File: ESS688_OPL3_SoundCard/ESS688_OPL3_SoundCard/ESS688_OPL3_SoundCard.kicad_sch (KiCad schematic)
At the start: 1 part, among them J1 Bus_ISA_16bit

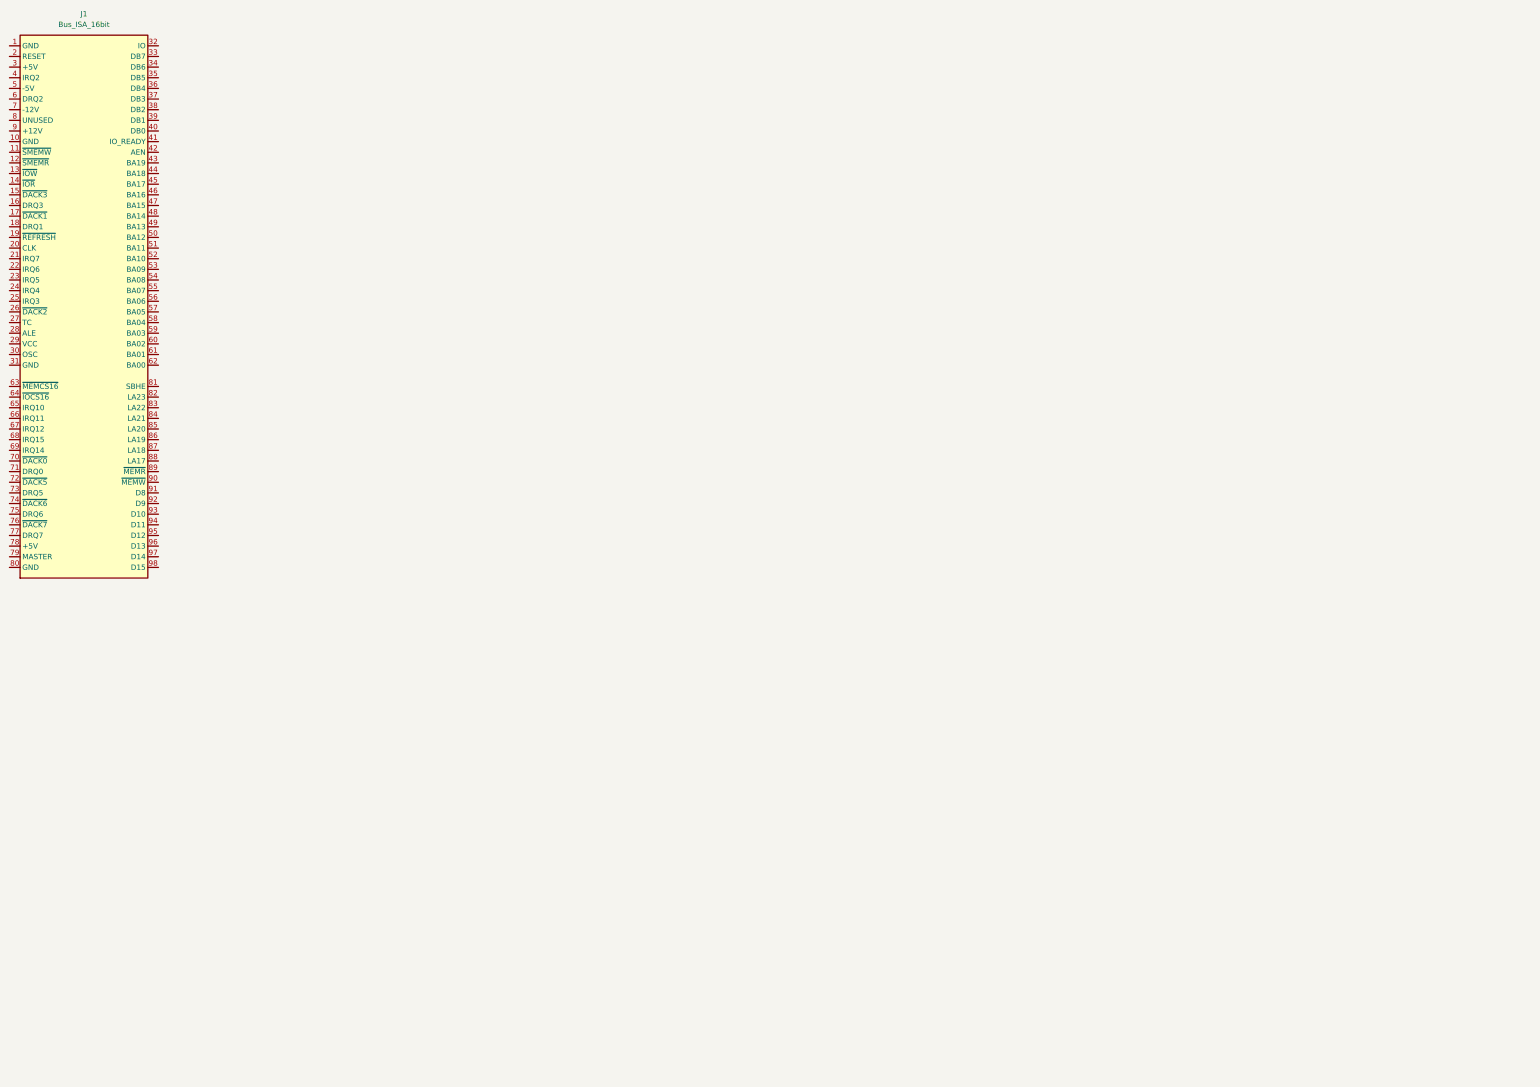
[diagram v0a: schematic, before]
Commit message: ES688 symbol updated, added more symbols to schematic
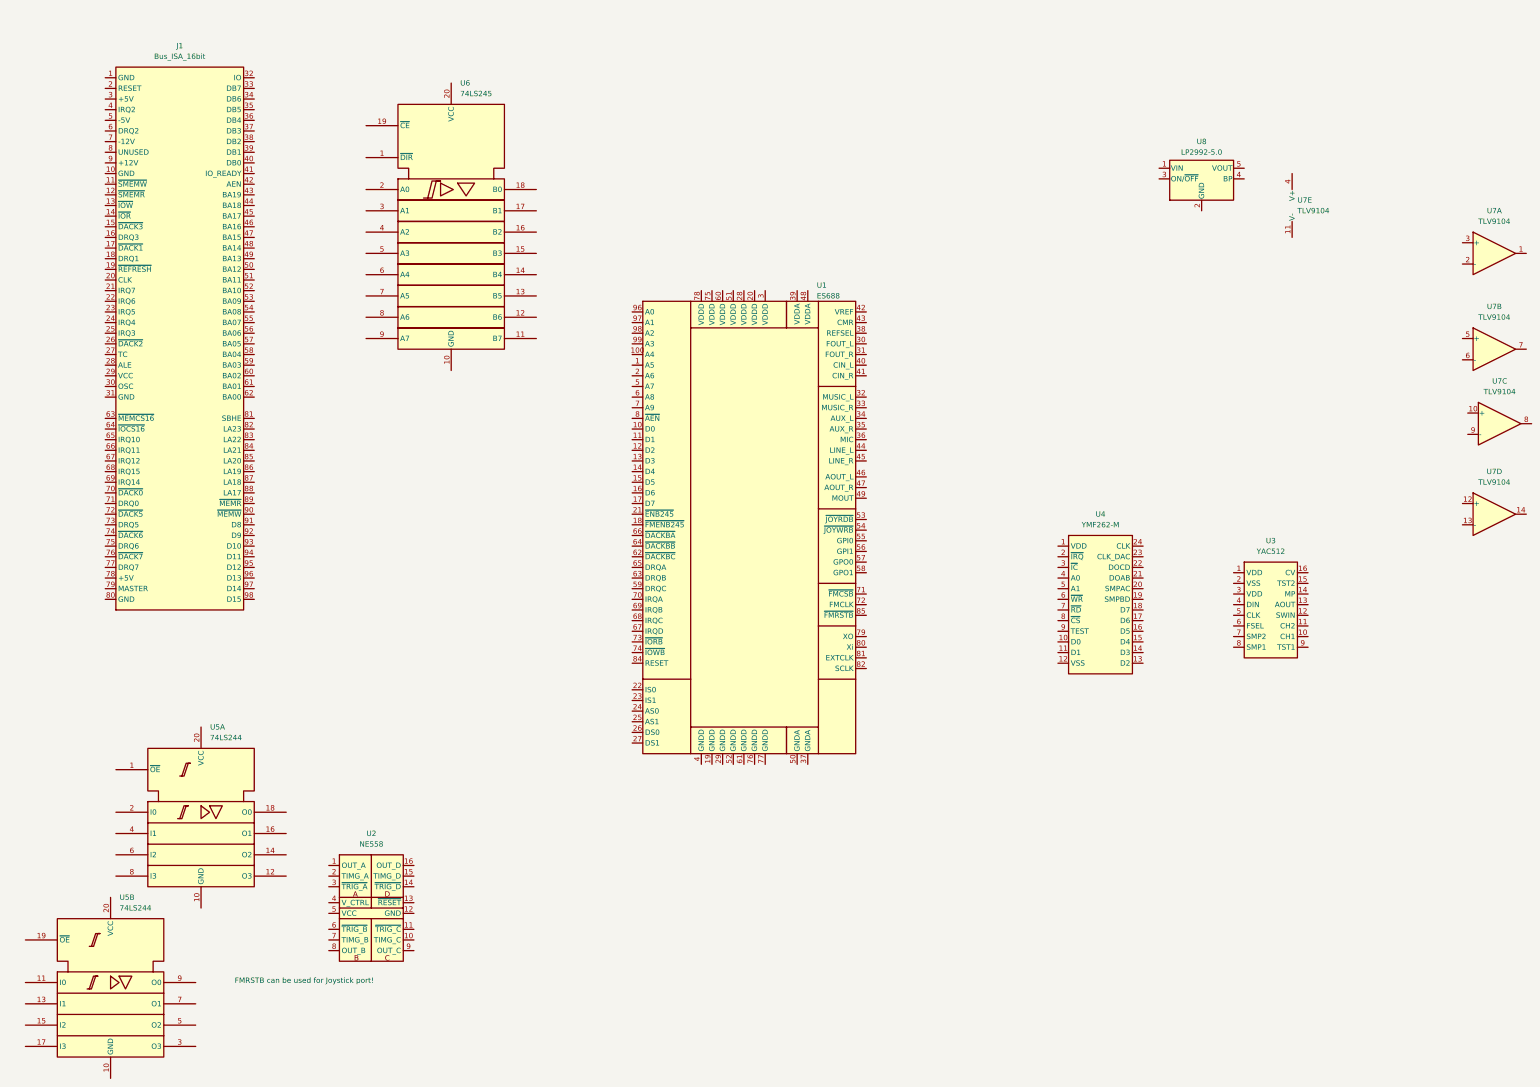
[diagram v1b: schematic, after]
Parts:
- added U1: ES688, Package_QFP:PQFP-100_14x20mm_P0.65mm, symbol ESS688_OPL3_SoundCard:ES688
- added U2: NE558, Package_DIP:DIP-16_W7.62mm, symbol ESS688_OPL3_SoundCard:NE558
- added U3: YAC512, Package_SO:SO-16_5.3x10.2mm_P1.27mm, symbol ESS688_OPL3_SoundCard:YAC512
- added U4: YMF262-M, Package_SO:SOP-24_7.5x15.4mm_P1.27mm, symbol ESS688_OPL3_SoundCard:YMF262-M
- added U5: 74LS244, Package_TO_SOT_SMD:SOT-23-5, symbol 74xx_IEEE:74LS244
- added U6: 74LS245, symbol 74xx_IEEE:74LS245
- added U7: TLV9104, Package_DFN_QFN:Texas_DSQ0010A_WSON-10-1EP_2x2mm_P0.4mm_EP0.9x1.5mm, symbol Amplifier_Operational:TL084
- added U8: LP2992-5.0, Package_TO_SOT_SMD:SOT-23-5, symbol Regulator_Linear:LP2985-5.0
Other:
- note added: "FMRSTB can be used for Joystick port!"
- moved on the sheet: J1

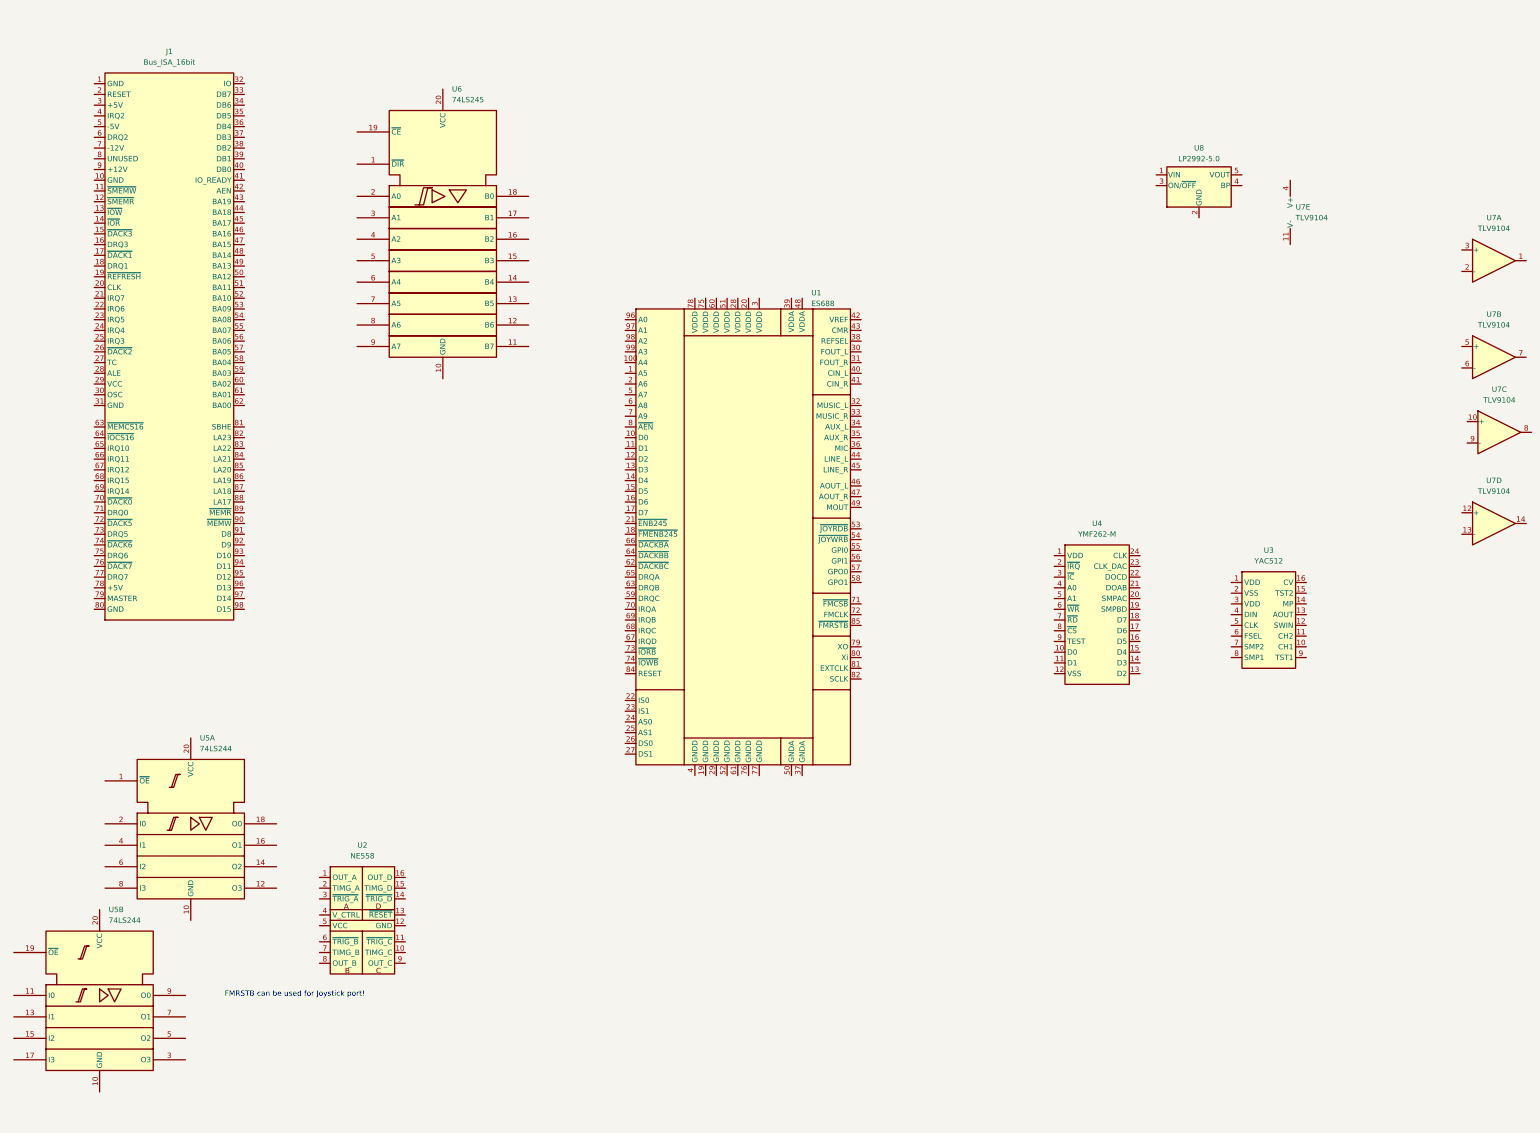
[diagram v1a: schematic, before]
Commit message: busses drawn, digital part 90% finished
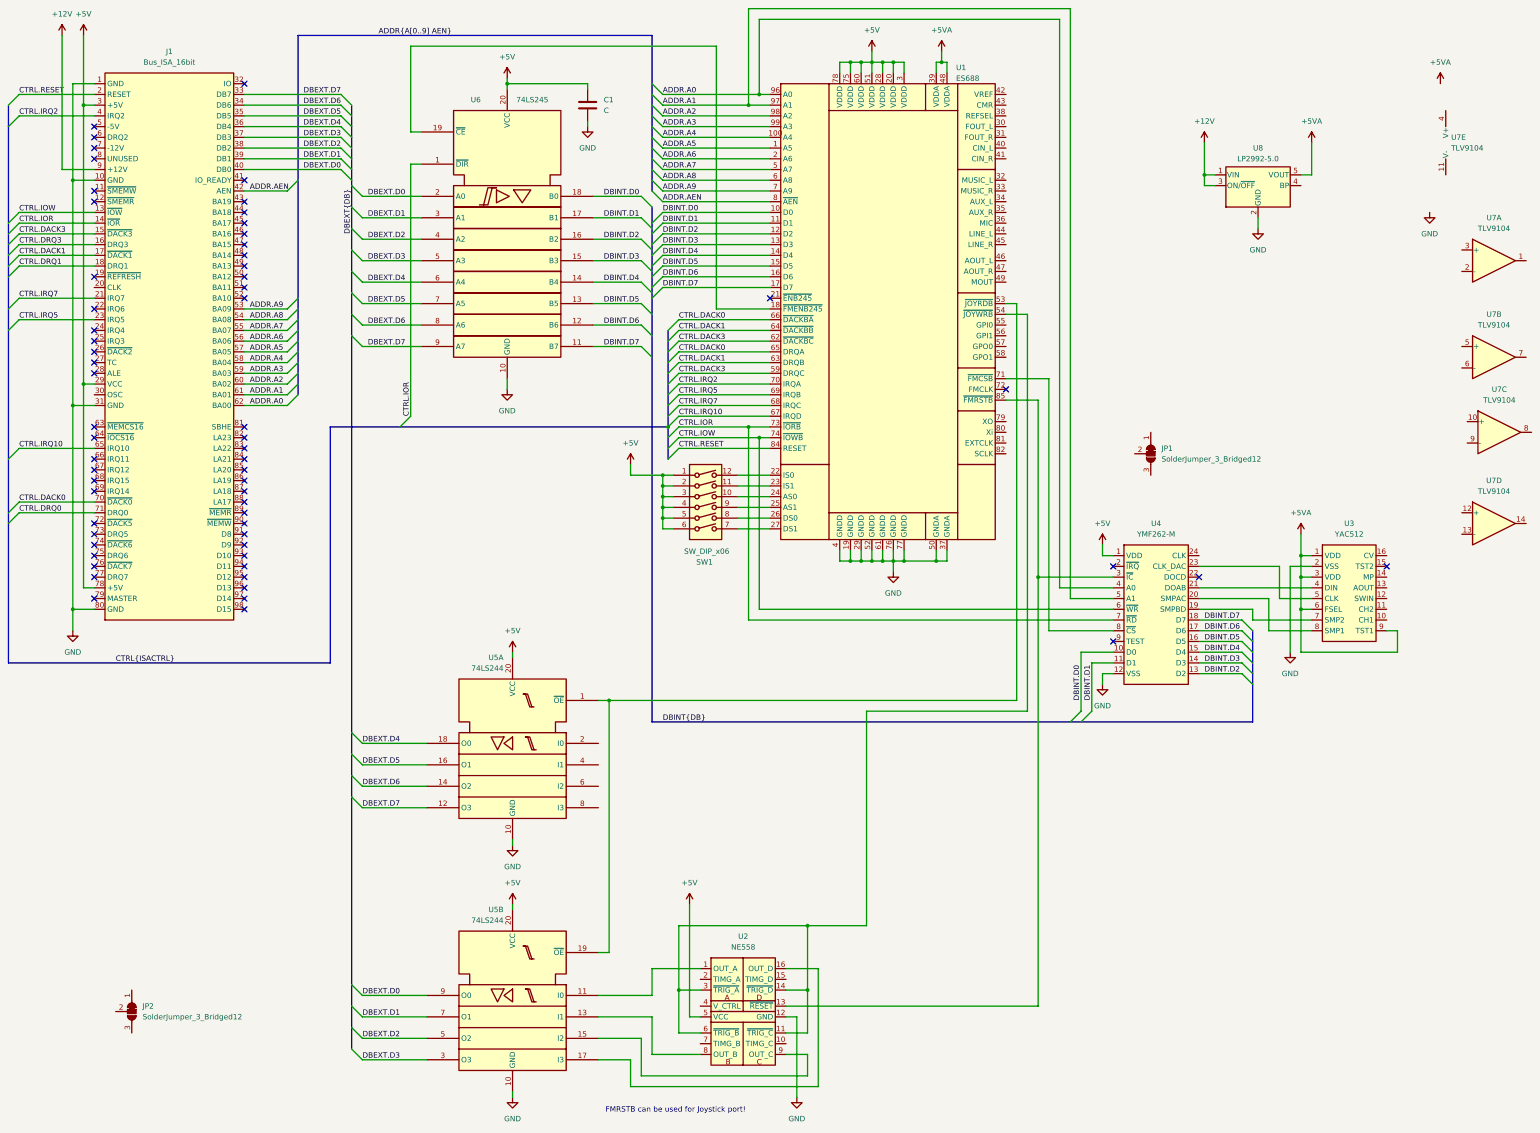
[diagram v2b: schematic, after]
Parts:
- added C1: C, symbol Device:C
- added JP1, JP2: SolderJumper_3_Bridged12, Package_SON:WSON-8-1EP_6x5mm_P1.27mm_EP3.4x4mm, symbol Jumper:SolderJumper_3_Bridged12
- added SW1: SW_DIP_x06, Package_SON:WSON-8-1EP_6x5mm_P1.27mm_EP3.4x4mm, symbol Switch:SW_DIP_x06
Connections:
- net at U5.1 (~{OE}): now also U1.53 (~{JOYRDB}), U5.19 (~{OE})
- net GND: now reaches U5.10 (GND)
- net GND: now also J1.1 (GND), J1.10 (GND), J1.31 (GND), J1.80 (GND), U1.19 (GNDD), U1.29 (GNDD), U1.37 (GNDA), U1.4 (GNDD), U1.50 (GNDA), U1.52 (GNDD), U1.61 (GNDD), U1.76 (GNDD), U1.77 (GNDD), U2.12 (GND), U3.2 (VSS), U4.12 (VSS), U5.10 (GND), U6.10 (GND), U8.2 (GND), C1.2
- net DBEXT.D7: now reaches U5.12 (O3)
- net DBEXT.D7: now also J1.33 (DB7), U6.9 (A7)
- net DBEXT.D6: now reaches U5.14 (O2)
- net DBEXT.D6: now also J1.34 (DB6), U6.8 (A6)
- net DBEXT.D5: now reaches U5.16 (O1)
- net DBEXT.D5: now also J1.35 (DB5), U6.7 (A5)
- net DBEXT.D4: now reaches U5.18 (O0)
- net DBEXT.D4: now also J1.36 (DB4), U6.6 (A4)
- net +5V: now reaches U5.20 (VCC)
- net +5V: now also J1.29 (VCC), J1.3 (+5V), J1.78 (+5V), U1.20 (VDDD), U1.28 (VDDD), U1.3 (VDDD), U1.51 (VDDD), U1.60 (VDDD), U1.75 (VDDD), U1.78 (VDDD), U2.5 (VCC), U4.1 (VDD), U5.20 (VCC), U6.20 (VCC), C1.1, SW1.1, SW1.2, SW1.3, SW1.4, SW1.5, SW1.6
- net CTRL.IOW: now reaches J1.13 (~{IOW})
- net CTRL.IOW: now also U1.74 (~{IOWB}), U4.6 (~{WR})
- net CTRL.IOR: now reaches J1.14 (~{IOR})
- net CTRL.IOR: now also U1.73 (~{IORB}), U4.7 (~{RD}), U6.1 (~{DIR})
- net CTRL.DACK3: now reaches J1.15 (~{DACK3})
- net CTRL.DACK3: now also U1.59 (DRQC), U1.62 (~{DACKBC})
- net CTRL.DRQ3: now reaches J1.16 (DRQ3)
- net CTRL.DACK1: now reaches J1.17 (~{DACK1})
- net CTRL.DACK1: now also U1.63 (DRQB), U1.64 (~{DACKBB})
- net CTRL.DRQ1: now reaches J1.18 (DRQ1)
- net CTRL.RESET: now reaches J1.2 (RESET)
- net CTRL.RESET: now also U1.84 (RESET)
- net CTRL.IRQ7: now reaches J1.21 (IRQ7)
- net CTRL.IRQ7: now also U1.68 (IRQC)
- net CTRL.IRQ5: now reaches J1.23 (IRQ5)
- net CTRL.IRQ5: now also U1.69 (IRQB)
- net DBEXT.D3: now reaches J1.37 (DB3)
- net DBEXT.D3: now also U5.3 (O3), U6.5 (A3)
- net DBEXT.D2: now reaches J1.38 (DB2)
- net DBEXT.D2: now also U5.5 (O2), U6.4 (A2)
- net DBEXT.D1: now reaches J1.39 (DB1)
- net DBEXT.D1: now also U5.7 (O1), U6.3 (A1)
- net CTRL.IRQ2: now reaches J1.4 (IRQ2)
- net CTRL.IRQ2: now also U1.70 (IRQA)
- net DBEXT.D0: now reaches J1.40 (DB0)
- net DBEXT.D0: now also U5.9 (O0), U6.2 (A0)
- net ADDR.AEN: now reaches J1.42 (AEN)
- net ADDR.AEN: now also U1.8 (~{AEN})
- net ADDR.A9: now reaches J1.53 (BA09)
- net ADDR.A9: now also U1.7 (A9)
- net ADDR.A8: now reaches J1.54 (BA08)
- net ADDR.A8: now also U1.6 (A8)
- net ADDR.A7: now reaches J1.55 (BA07)
- net ADDR.A7: now also U1.5 (A7)
- net ADDR.A6: now reaches J1.56 (BA06)
- net ADDR.A6: now also U1.2 (A6)
- net ADDR.A5: now reaches J1.57 (BA05)
- net ADDR.A5: now also U1.1 (A5)
- net ADDR.A4: now reaches J1.58 (BA04)
- net ADDR.A4: now also U1.100 (A4)
- net ADDR.A3: now reaches J1.59 (BA03)
- net ADDR.A3: now also U1.99 (A3)
- net ADDR.A2: now reaches J1.60 (BA02)
- net ADDR.A2: now also U1.98 (A2)
- net ADDR.A1: now reaches J1.61 (BA01)
- net ADDR.A1: now also U1.97 (A1), U4.5 (A1)
- net ADDR.A0: now reaches J1.62 (BA00)
- net ADDR.A0: now also U1.96 (A0), U4.4 (A0)
- net CTRL.IRQ10: now reaches J1.65 (IRQ10)
- net CTRL.IRQ10: now also U1.67 (IRQD)
- net CTRL.DACK0: now reaches J1.70 (~{DACK0})
- net CTRL.DACK0: now also U1.65 (DRQA), U1.66 (~{DACKBA})
- net CTRL.DRQ0: now reaches J1.71 (DRQ0)
- net +12V: now reaches J1.9 (+12V)
- net +12V: now also U8.1 (VIN), U8.3 (ON/~{OFF})
- net at U5.11 (I0): now also U2.1 (OUT_A)
- net at U5.13 (I1): now also U2.8 (OUT_B)
- net at U5.15 (I2): now also U2.9 (OUT_C)
- net at U5.17 (I3): now also U2.16 (OUT_D)
- net +5VA: now reaches U3.1 (VDD)
- net +5VA: now also U1.39 (VDDA), U1.48 (VDDA), U3.3 (VDD), U3.6 (FSEL), U3.9 (TST1), U8.5 (VOUT)
- net at U3.4 (DIN): now also U4.21 (DOAB)
- net at U3.5 (CLK): now also U4.23 (CLK_DAC)
- net at U3.7 (SMP2): now also U4.19 (SMPBD)
- net at U3.8 (SMP1): now also U4.20 (SMPAC)
- net at U2.11 (~{TRIG_C}): now also U1.54 (~{JOYWRB}), U2.14 (~{TRIG_D}), U2.3 (~{TRIG_A}), U2.6 (~{TRIG_B})
- net at U2.13 (~{RESET}): now also U1.85 (~{FMRSTB}), U4.3 (~{IC})
- net DBINT.D7: now reaches U6.11 (B7)
- net DBINT.D7: now also U1.17 (D7), U4.18 (D7)
- net DBINT.D6: now reaches U6.12 (B6)
- net DBINT.D6: now also U1.16 (D6), U4.17 (D6)
- net DBINT.D5: now reaches U6.13 (B5)
- net DBINT.D5: now also U1.15 (D5), U4.16 (D5)
- net DBINT.D4: now reaches U6.14 (B4)
- net DBINT.D4: now also U1.14 (D4), U4.15 (D4)
- net DBINT.D3: now reaches U6.15 (B3)
- net DBINT.D3: now also U1.13 (D3), U4.14 (D3)
- net DBINT.D2: now reaches U6.16 (B2)
- net DBINT.D2: now also U1.12 (D2), U4.13 (D2)
- net DBINT.D1: now reaches U6.17 (B1)
- net DBINT.D1: now also U1.11 (D1), U4.11 (D1)
- net DBINT.D0: now reaches U6.18 (B0)
- net DBINT.D0: now also U1.10 (D0), U4.10 (D0)
- net at U6.19 (~{CE}): now also U1.18 (~{FMENB245})
- net at U4.8 (~{CS}): now also U1.71 (~{FMCSB})
- net at U1.22 (IS0): now also SW1.12
- net at U1.23 (IS1): now also SW1.11
- net at U1.24 (AS0): now also SW1.10
- net at U1.25 (AS1): now also SW1.9
- net at U1.26 (DS0): now also SW1.8
- net at U1.27 (DS1): now also SW1.7
- no-connect marks 0 -> 62
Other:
- moved on the sheet: U1, U2, U3, U4, U5A, U5B, U6, U7E, U8
